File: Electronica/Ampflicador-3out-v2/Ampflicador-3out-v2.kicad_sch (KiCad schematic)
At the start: 32 parts, among them Q1 MPF102, SW1 SW_DPST_x2, SW2 SW_DPST_x2, U1 LM386

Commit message: Amp v2 sin acordate
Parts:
- removed Bass1, Gain1, Input1, Input2, Input3, Output-Jack-6.1, Output-Speaker1, Power-Input1: Screw_Terminal_01x02, Connector_Molex:Molex_KK-254_AE-6410-02A_1x02_P2.54mm_Vertical, symbol Connector:Screw_Terminal_01x02
- removed Vol1: Screw_Terminal_01x03, Connector_Molex:Molex_KK-254_AE-6410-03A_1x03_P2.54mm_Vertical, symbol Connector:Screw_Terminal_01x03
- added BT1: Power Input, Connector_Molex:Molex_KK-254_AE-6410-02A_1x02_P2.54mm_Vertical, symbol Device:Battery
- added J1: Jack 6.5, Connector_Molex:Molex_KK-254_AE-6410-02A_1x02_P2.54mm_Vertical, symbol Connector_Audio:AudioJack2_Ground
- added LS1: Speaker, Connector_Molex:Molex_KK-254_AE-6410-02A_1x02_P2.54mm_Vertical, symbol Device:Speaker
- added P1: Piezo 1, Connector_Molex:Molex_KK-254_AE-6410-02A_1x02_P2.54mm_Vertical, symbol Device:Crystal
- added P2, P3: Piezo 2, Connector_Molex:Molex_KK-254_AE-6410-02A_1x02_P2.54mm_Vertical, symbol Device:Crystal
- added RV1: Volume, Connector_Molex:Molex_KK-254_AE-6410-03A_1x03_P2.54mm_Vertical, symbol Device:R_Potentiometer
- added RV2: Gain, Connector_Molex:Molex_KK-254_AE-6410-02A_1x02_P2.54mm_Vertical, symbol Device:R_Potentiometer
- added RV3: Bass, Connector_Molex:Molex_KK-254_AE-6410-02A_1x02_P2.54mm_Vertical, symbol Device:R_Potentiometer
- added SW3: SW_SPDT, Connector_Molex:Molex_KK-254_AE-6410-03A_1x03_P2.54mm_Vertical, symbol Switch:SW_SPDT
- renumbered Output-Jack-3.1 to Output-Jack-3.5
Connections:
- net GND: now also Output-Jack-3.5.S, BT1.2 (-), J1.G, J1.S, LS1.2, P3.1, RV1.3
- net at SW2.1 (A): now also P1.1, P2.2
- net at C10.1: now also P1.2
- net at U1.1 (GAIN): now also RV2.2, RV3.1
- net at C8.1: now also RV3.2
- net at Output-Jack-3.5.TN: now also SW3.2 (B)
- net at C12.2: now also RV1.1
- net at U1.3 (+): now also RV1.2
- net at C6.1: now also RV2.1
- net at SW1.1 (A): now also BT1.1 (+)
- new net: P2.1, P3.2
- new net: LS1.1, SW3.3 (C)
- new net: J1.T, SW3.1 (A)
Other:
- moved on the sheet: C10, C12, C2, C3, C9, R3, R4, SW1A, SW2A

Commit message: Amp creo que para imprimir
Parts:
- removed SW3: SW_SPDT, Connector_Molex:Molex_KK-254_AE-6410-03A_1x03_P2.54mm_Vertical, symbol Switch:SW_SPDT
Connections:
- net GND: no longer Output-Jack-3.5.S
- net at LS1.1: now also J1.T, Output-Jack-3.5.SN, Output-Jack-3.5.TN
- net at C9.2, Output-Jack-3.5.T: now also Output-Jack-3.5.S
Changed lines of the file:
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@@
+	)
+	(junction
+		(at 182.88 86.36)
+		(diameter 0)
+		(color 0 0 0 0)
 	)
 	(junction
@@
 	)
 	(junction
+		(at 181.61 101.6)
+		(diameter 0)
+		(color 0 0 0 0)
+	)
+	(junction
+		(at 181.61 88.9)
+		(diameter 0)
+		(color 0 0 0 0)
+	)
+	(junction
 		(at 66.04 118.11)
 		(diameter 0)
@@
 	)
 	(junction
-		(at 194.31 93.98)
-		(diameter 0)
-		(color 0 0 0 0)
-	)
-	(junction
 		(at 130.81 66.04)
 		(diameter 0)
@@
 	(wire
 		(pts
-			(xy 181.61 91.44) (xy 181.61 83.82)
+			(xy 181.61 88.9) (xy 181.61 101.6)
 		)
 		(stroke
@@
 	(wire
 		(pts
-			(xy 187.96 91.44) (xy 187.96 93.98)
-		)
-		(stroke
-			(width 0)
-			(type default)
-		)
-	)
-	(wire
-		(pts
 			(xy 162.56 86.36) (xy 170.18 86.36)
 		)
@@
 	(wire
 		(pts
-			(xy 187.96 93.98) (xy 194.31 93.98)
-		)
-		(stroke
-			(width 0)
-			(type default)
-		)
-	)
-	(wire
-		(pts
 			(xy 69.85 67.31) (xy 76.2 67.31)
 		)
@@
 	(wire
 		(pts
-			(xy 179.07 101.6) (xy 179.07 111.76)
+			(xy 181.61 101.6) (xy 181.61 111.76)
 		)
 		(stroke
@@
 	(wire
 		(pts
-			(xy 184.15 101.6) (xy 189.23 101.6)
+			(xy 181.61 88.9) (xy 181.61 83.82)
 		)
 		(stroke
@@
 	(wire
 		(pts
+			(xy 182.88 91.44) (xy 187.96 91.44)
+		)
+		(stroke
+			(width 0)
+			(type default)
+		)
+	)
+	(wire
+		(pts
 			(xy 152.4 86.36) (xy 162.56 86.36)
 		)
@@
 	(wire
 		(pts
+			(xy 181.61 101.6) (xy 189.23 101.6)
+		)
+		(stroke
+			(width 0)
+			(type default)
+		)
+	)
+	(wire
+		(pts
 			(xy 128.27 118.11) (xy 120.65 118.11)
 		)
@@
 	(wire
 		(pts
+			(xy 182.88 86.36) (xy 187.96 86.36)
+		)
+		(stroke
+			(width 0)
+			(type default)
+		)
+	)
+	(wire
+		(pts
 			(xy 114.3 88.9) (xy 123.19 88.9)
 		)
@@
 	(wire
 		(pts
+			(xy 181.61 88.9) (xy 187.96 88.9)
+		)
+		(stroke
+			(width 0)
+			(type default)
+		)
+	)
+	(wire
+		(pts
 			(xy 130.81 95.25) (xy 130.81 93.98)
 		)
@@
 	(wire
 		(pts
-			(xy 177.8 86.36) (xy 187.96 86.36)
+			(xy 177.8 86.36) (xy 182.88 86.36)
 		)
 		(stroke
@@
 	(wire
 		(pts
+			(xy 182.88 86.36) (xy 182.88 91.44)
+		)
+		(stroke
+			(width 0)
+			(type default)
+		)
+	)
+	(wire
+		(pts
 			(xy 76.2 118.11) (xy 110.49 118.11)
 		)
@@
 	(wire
 		(pts
-			(xy 179.07 111.76) (xy 189.23 111.76)
+			(xy 181.61 111.76) (xy 189.23 111.76)
 		)
 		(stroke
@@
 					(unit 1)
 				)
-			)
-		)
-	)
-	(symbol
-		(lib_id "Switch:SW_SPDT")
-		(at 181.61 96.52 270)
-		(unit 1)
-		(exclude_from_sim no)
-		(in_bom yes)
-		(on_board yes)
-		(dnp no)
-		(property "Reference" "SW3"
-			(at 170.434 94.742 90)
-			(effects
-				(font
-					(size 1.27 1.27)
-				)
-				(justify left)
-			)
-		)
-		(property "Value" "SW_SPDT"
-			(at 167.894 97.536 90)
-			(effects
-				(font
-					(size 1.27 1.27)
-				)
-				(justify left)
-			)
-		)
-		(property "Footprint" "Connector_Molex:Molex_KK-254_AE-6410-03A_1x03_P2.54mm_Vertical"
-			(at 181.61 96.52 0)
-			(effects
-				(font
-					(size 1.27 1.27)
-				)
-				(hide yes)
-			)
-		)
-		(property "Datasheet" "~"
-			(at 173.99 96.52 0)
-			(effects
-				(font
-					(size 1.27 1.27)
-				)
-				(hide yes)
-			)
-		)
-		(property "Description" "Switch, single pole double throw"
-			(at 181.61 96.52 0)
-			(effects
-				(font
-					(size 1.27 1.27)
-				)
-				(hide yes)
-			)
-		)
-		(pin "1"
-		)
-		(pin "2"
-		)
-		(pin "3"
-		)
-		(instances
-			(project "Ampflicador-3out-v2"
-				(path "/5f6a0c50-88ca-432f-8e17-5a05c9c3ac4b"
-					(reference "SW3")
-					(unit 1)
-				)

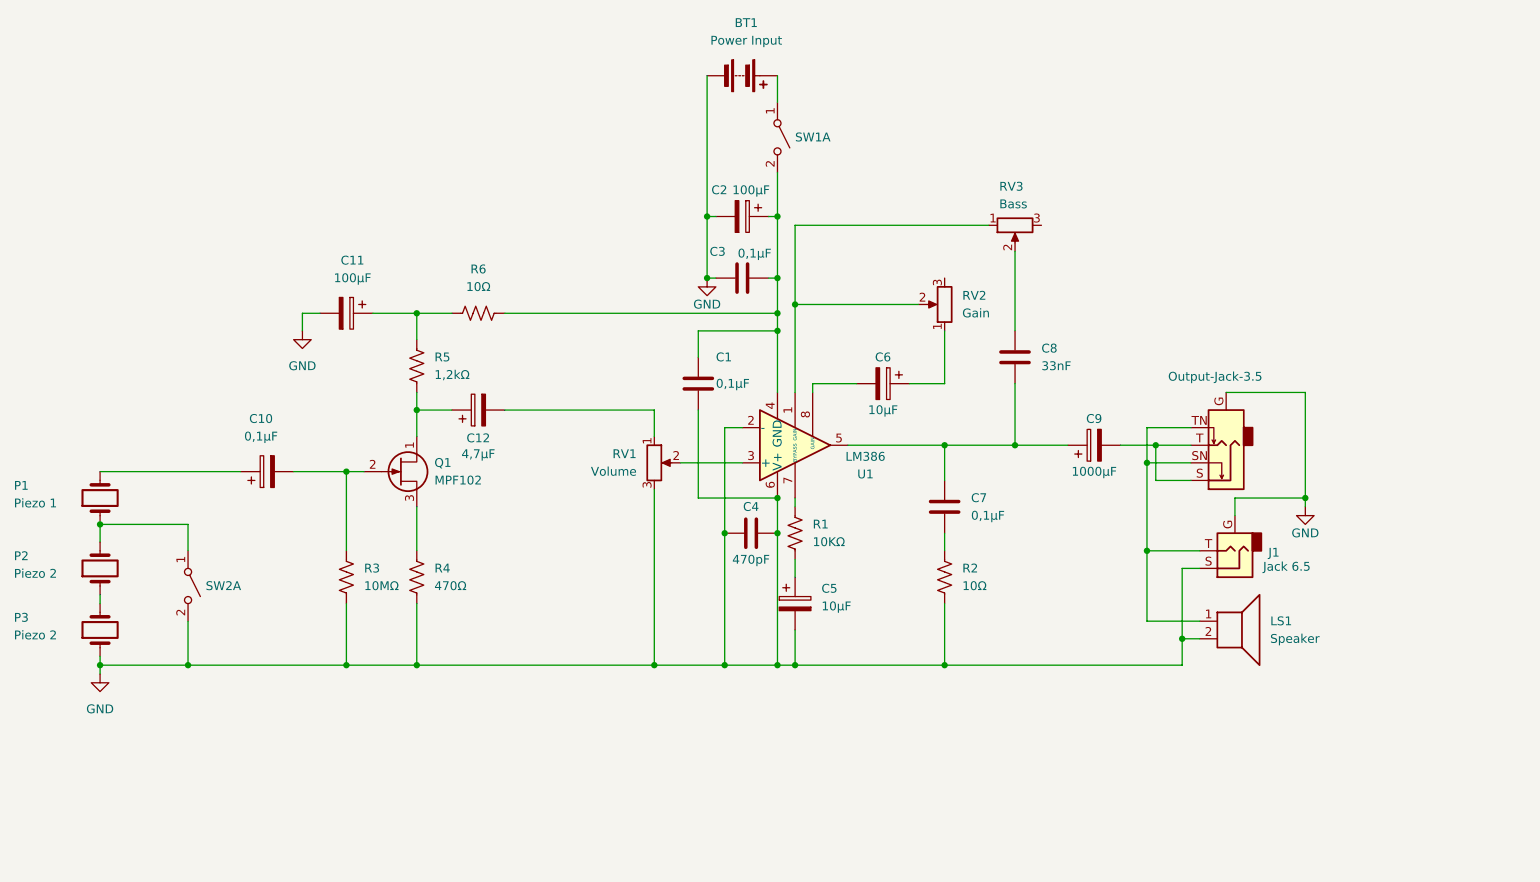
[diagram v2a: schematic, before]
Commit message: Amp V2 con Led
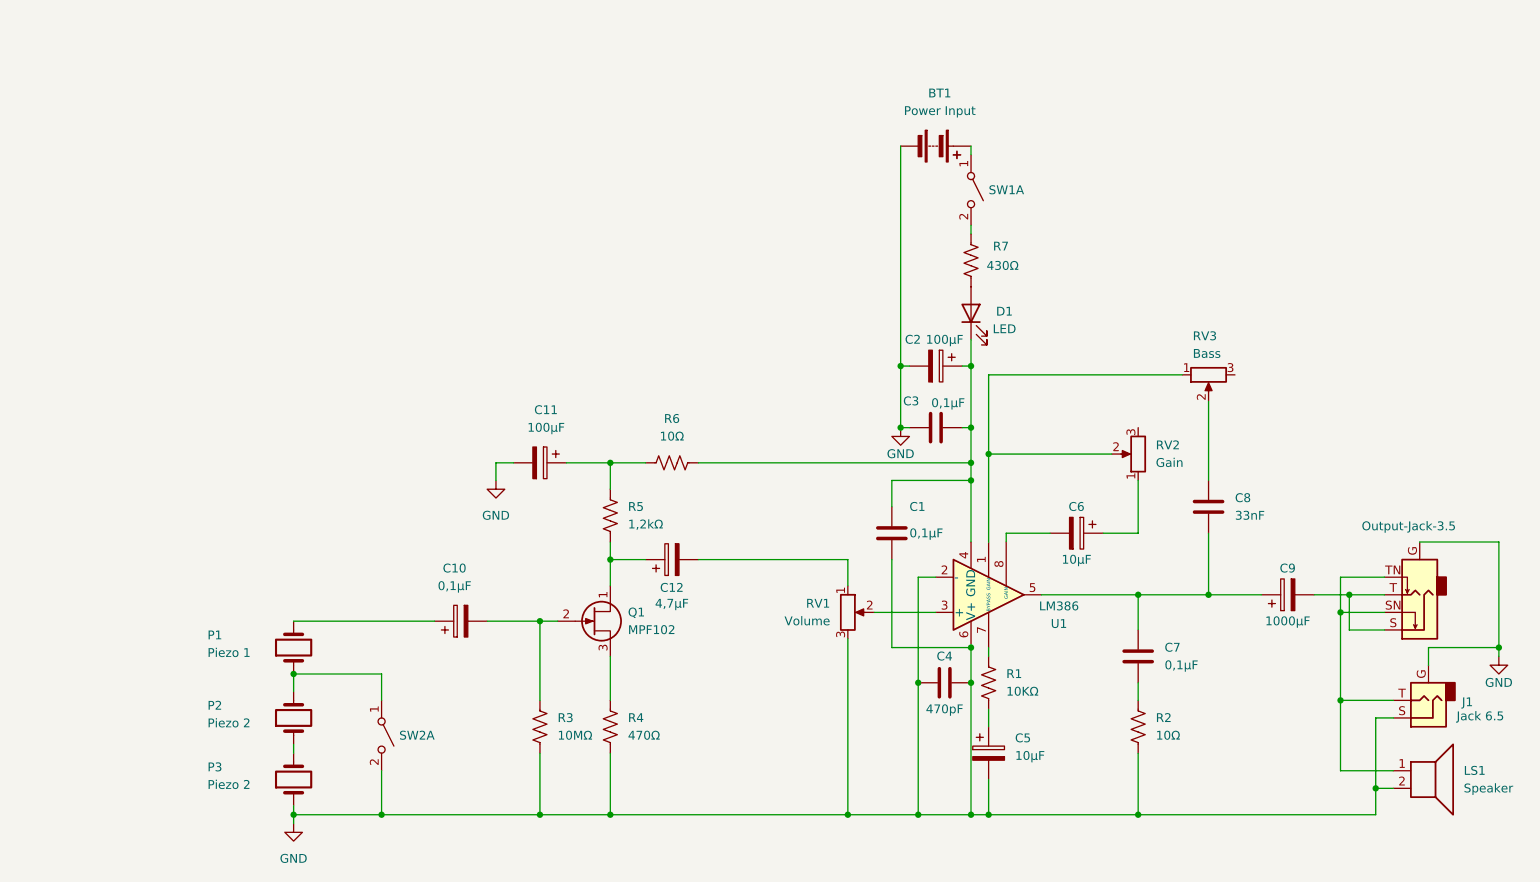
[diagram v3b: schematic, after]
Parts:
- added D1: LED, Connector_Molex:Molex_KK-254_AE-6410-02A_1x02_P2.54mm_Vertical, symbol Device:LED
- added R7: 430Ω, Resistor_THT:R_Axial_DIN0204_L3.6mm_D1.6mm_P7.62mm_Horizontal, symbol Device:R_US
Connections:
- net at C1.1, C2.1, C3.2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: now also D1.1 (K); no longer SW1.2 (B)
- new net: R7.1, SW1.2 (B)
- new net: D1.2 (A), R7.2
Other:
- moved on the sheet: BT1, C1, C10, C11, C12, C2, C3, C4, C5, C6, C7, C8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
